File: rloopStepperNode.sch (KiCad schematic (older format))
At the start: 0 parts

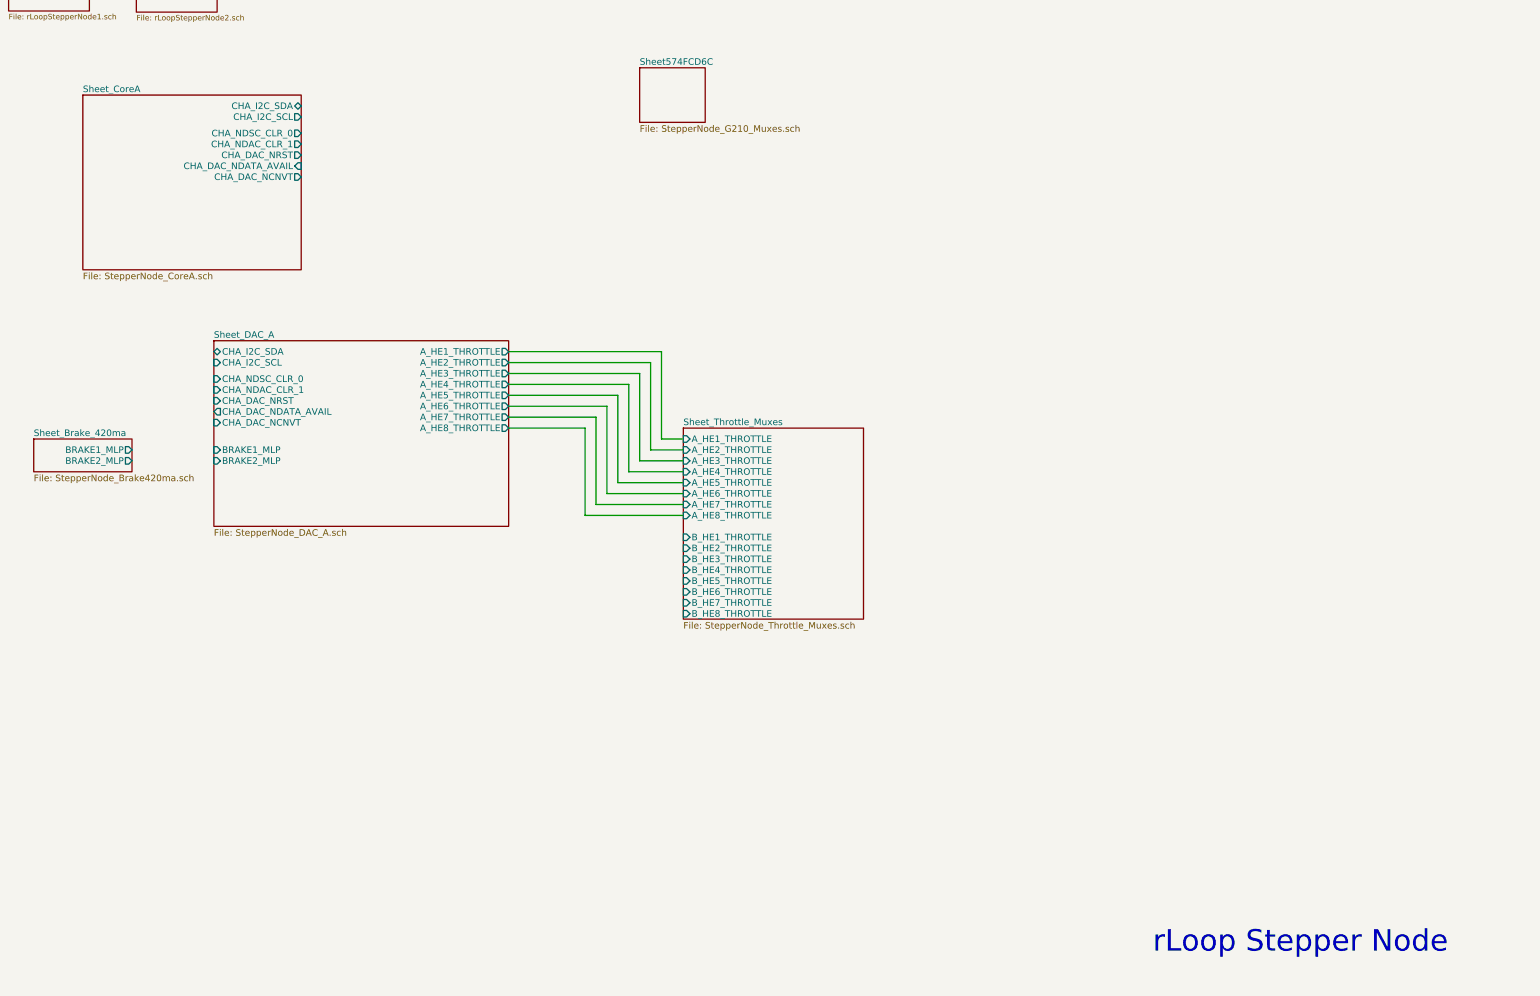
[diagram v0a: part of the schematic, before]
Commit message: Setup DAC channel B
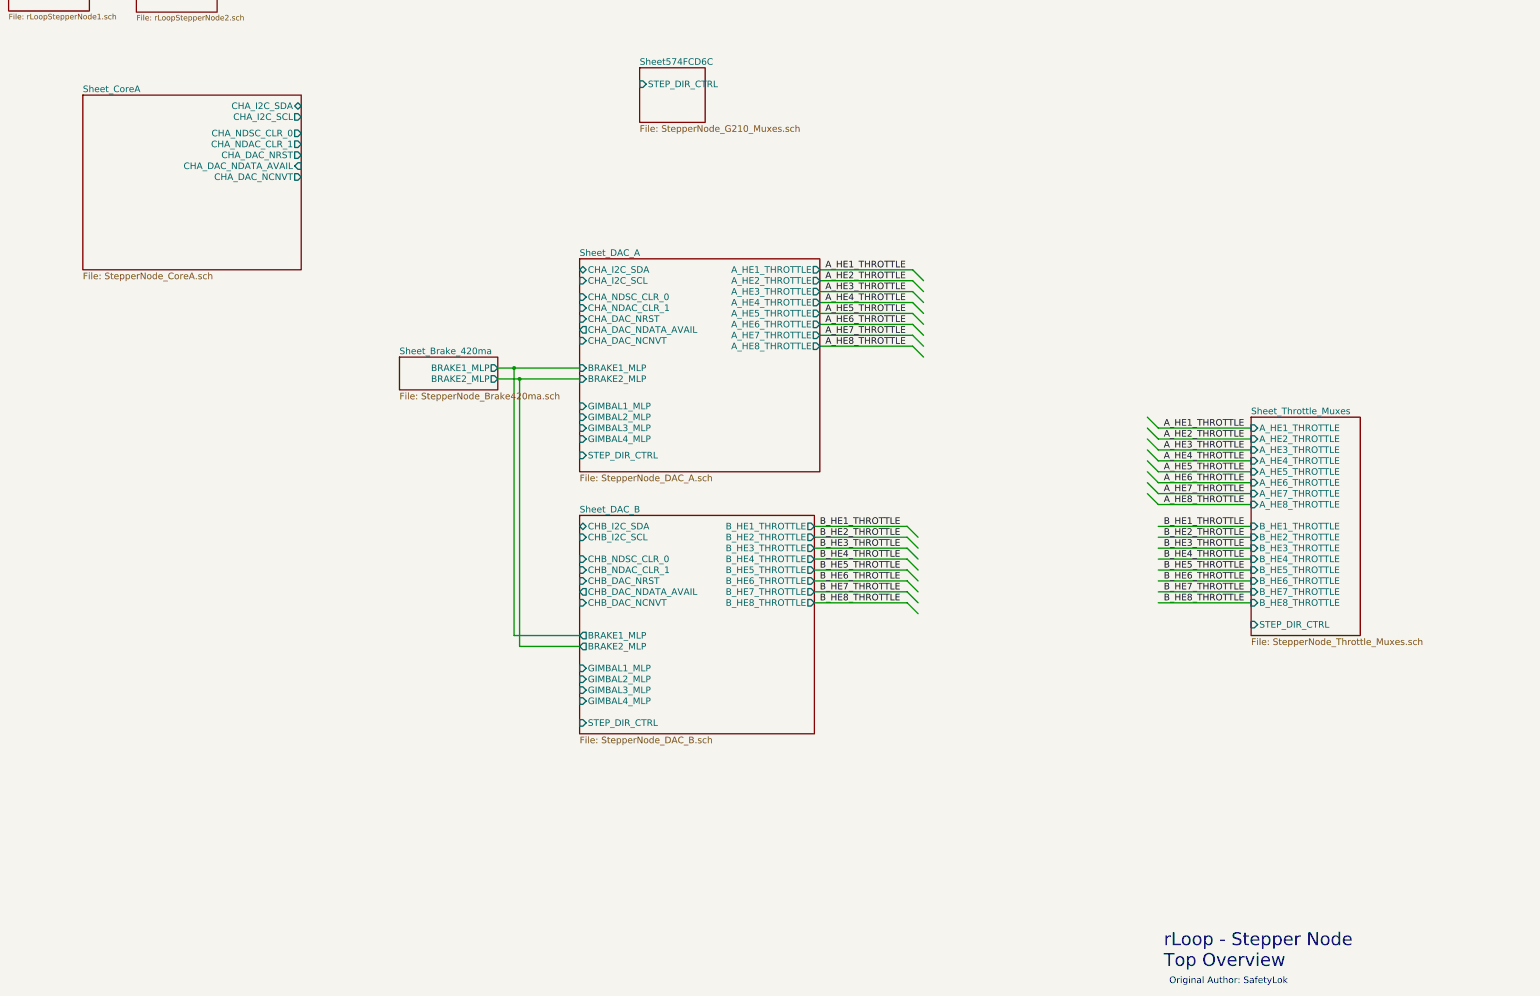
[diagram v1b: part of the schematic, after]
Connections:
- net labels added: A_HE1_THROTTLE, A_HE2_THROTTLE, A_HE3_THROTTLE, A_HE4_THROTTLE, A_HE5_THROTTLE, A_HE6_THROTTLE, A_HE7_THROTTLE, A_HE8_THROTTLE, B_HE1_THROTTLE, B_HE2_THROTTLE, B_HE3_THROTTLE, B_HE4_THROTTLE, B_HE5_THROTTLE, B_HE6_THROTTLE, B_HE7_THROTTLE, B_HE8_THROTTLE
- wire segments 24 -> 38
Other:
- note added: "Original Author: SafetyLok"
- note added: "rLoop - Stepper Node\nTop Overview\n"
- note removed: "rLoop Stepper Node\n"

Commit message: Setup Node Core Channel B
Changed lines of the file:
@@
 $Descr A3 16535 11693
 encoding utf-8
-Sheet 1 9
+Sheet 1 11
 Title "Top Level"
 Date ""
@@
 $EndDescr
 $Sheet
-S 1320 1150 740  430
-U 570CA0E2
-F0 "Sheet1" 50
-F1 "rLoopStepperNode1.sch" 50
-$EndSheet
-$Sheet
-S 2490 1150 740  440
-U 570DA2A0
-F0 "Sheet2" 50
-F1 "rLoopStepperNode2.sch" 50
-$EndSheet
-$Sheet
-S 7100 2100 600  500
+S 12700 3450 950  600
 U 574FCD6D
-F0 "Sheet574FCD6C" 60
+F0 "Sheet_G210_Muxes" 60
 F1 "StepperNode_G210_Muxes.sch" 60
-F2 "STEP_DIR_CTRL" I L 7100 2250 60
-$EndSheet
-$Sheet
-S 2000 2350 2000 1600
-U 57538643
-F0 "Sheet_CoreA" 60
-F1 "StepperNode_CoreA.sch" 60
-F2 "CHA_I2C_SDA" B R 4000 2450 60
-F3 "CHA_I2C_SCL" O R 4000 2550 60
-F4 "CHA_NDSC_CLR_0" O R 4000 2700 60
-F5 "CHA_NDAC_CLR_1" O R 4000 2800 60
-F6 "CHA_DAC_NRST" O R 4000 2900 60
-F7 "CHA_DAC_NDATA_AVAIL" I R 4000 3000 60
-F8 "CHA_DAC_NCNVT" O R 4000 3100 60
+F2 "STEP_DIR_CTRL" I L 12700 3600 60
 $EndSheet
 $Sheet
@@
 Text Notes 11950 10500 0    60   ~ 0
 Original Author: SafetyLok
+$Sheet
+S 12700 1800 900  1150
+U 5754F8C0
+F0 "Sheet_Gimbal_Sw" 60
+F1 "StepperNode_Gimbal_Switches.sch" 60
+$EndSheet
+$Sheet
+S 2000 5850 1250 2200
+U 57556833
+F0 "Sheet_CoreB" 60
+F1 "StepperNode_CoreB.sch" 60
+F2 "CHB_I2C_SDA" B R 3250 5950 60
+F3 "CHB_I2C_SCL" O R 3250 6050 60
+F4 "CHB_NDSC_CLR_0" O R 3250 6200 60
+F5 "CHB_NDAC_CLR_1" O R 3250 6300 60
+F6 "CHB_DAC_NRST" O R 3250 6400 60
+F7 "CHB_DAC_NDATA_AVAIL" I R 3250 6500 60
+F8 "CHB_DAC_NCNVT" O R 3250 6600 60
+F9 "CHB_STEP1_DIR" O R 3250 6800 60
+F10 "CHB_STEP1_STEP" O R 3250 6900 60
+F11 "CHB_STEP2_DIR" O R 3250 7000 60
+F12 "CHB_STEP2_STEP" O R 3250 7100 60
+F13 "CHB_STEP3_DIR" O R 3250 7200 60
+F14 "CHB_STEP3_STEP" O R 3250 7300 60
+F15 "CHB_STEP4_DIR" O R 3250 7400 60
+F16 "CHB_STEP4_STEP" O R 3250 7500 60
+F17 "CHB_STEP5_DIR" O R 3250 7600 60
+F18 "CHB_STEP5_STEP" O R 3250 7700 60
+F19 "CHB_STEP6_DIR" O R 3250 7800 60
+F20 "CHB_STEP6_STEP" O R 3250 7900 60
+$EndSheet
+$Sheet
+S 2000 2350 1250 2450
+U 57538643
+F0 "Sheet_CoreA" 60
+F1 "StepperNode_CoreA.sch" 60
+F2 "CHA_I2C_SDA" B R 3250 2450 60
+F3 "CHA_I2C_SCL" O R 3250 2550 60
+F4 "CHA_NDSC_CLR_0" O R 3250 2700 60
+F5 "CHA_NDAC_CLR_1" O R 3250 2800 60
+F6 "CHA_DAC_NRST" O R 3250 2900 60
+F7 "CHA_DAC_NDATA_AVAIL" I R 3250 3000 60
+F8 "CHA_DAC_NCNVT" O R 3250 3100 60
+F9 "CHA_STEP1_DIR" O R 3250 3350 60
+F10 "CHA_STEP1_STEP" O R 3250 3450 60
+F11 "CHA_STEP2_DIR" O R 3250 3550 60
+F12 "CHA_STEP2_STEP" O R 3250 3650 60
+F13 "CHA_STEP3_DIR" O R 3250 3750 60
+F14 "CHA_STEP3_STEP" O R 3250 3850 60
+F15 "CHA_STEP4_DIR" O R 3250 3950 60
+F16 "CHA_STEP4_STEP" O R 3250 4050 60
+F17 "CHA_STEP5_DIR" O R 3250 4150 60
+F18 "CHA_STEP5_STEP" O R 3250 4250 60
+F19 "CHA_STEP6_DIR" O R 3250 4350 60
+F20 "CHA_STEP6_STEP" O R 3250 4450 60
+$EndSheet
 $EndSCHEMATC

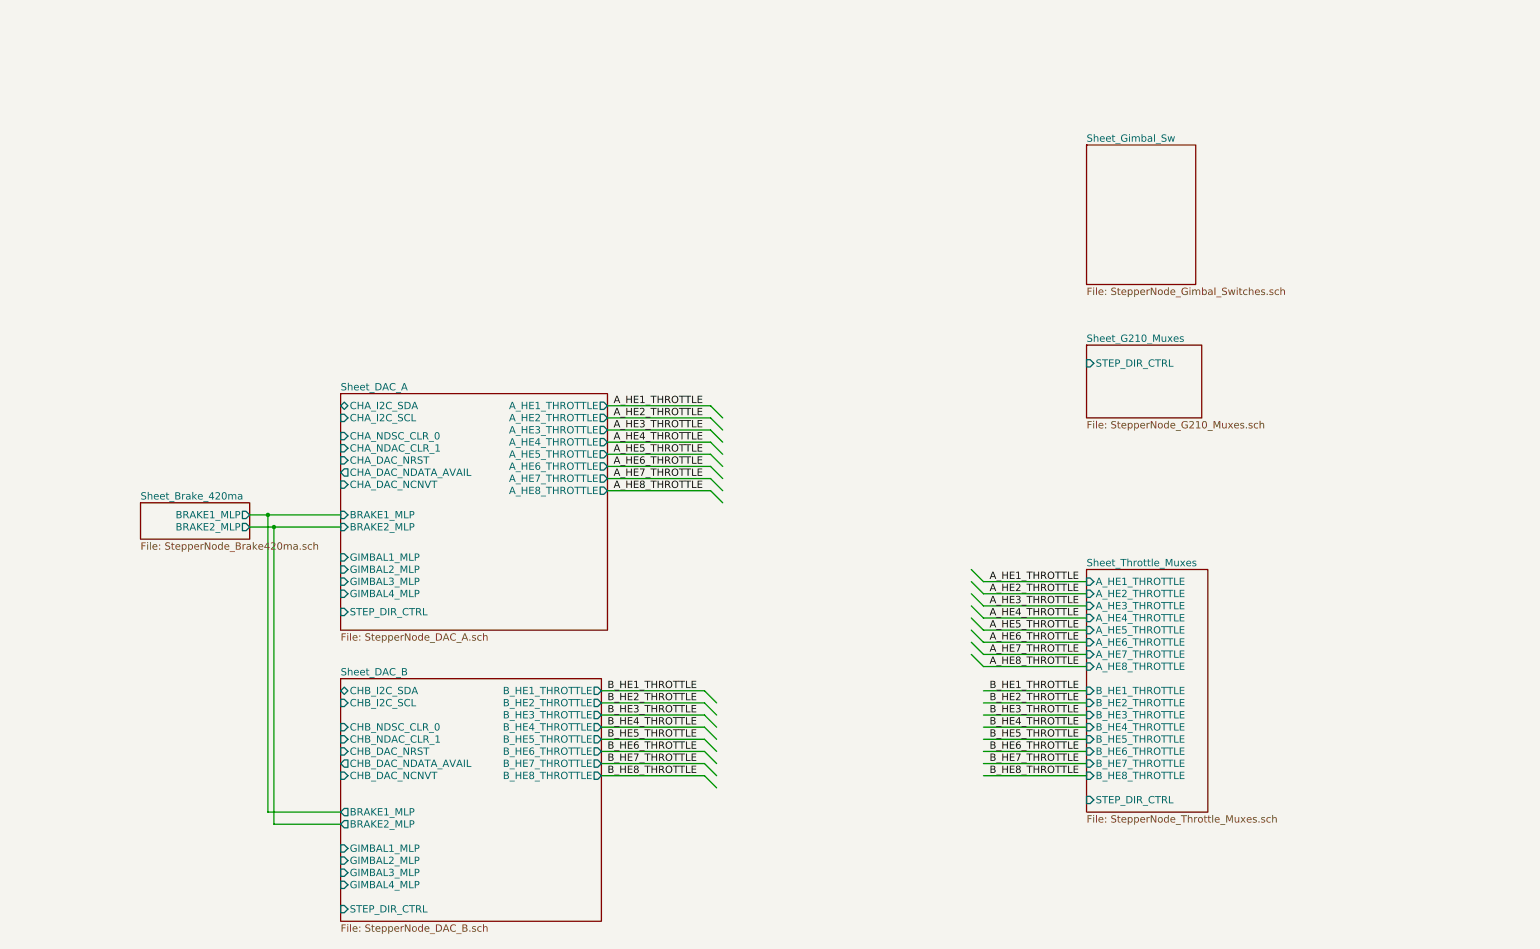
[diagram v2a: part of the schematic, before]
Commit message: Added Sheets for Gimbal, Pusher Interlock and Accels
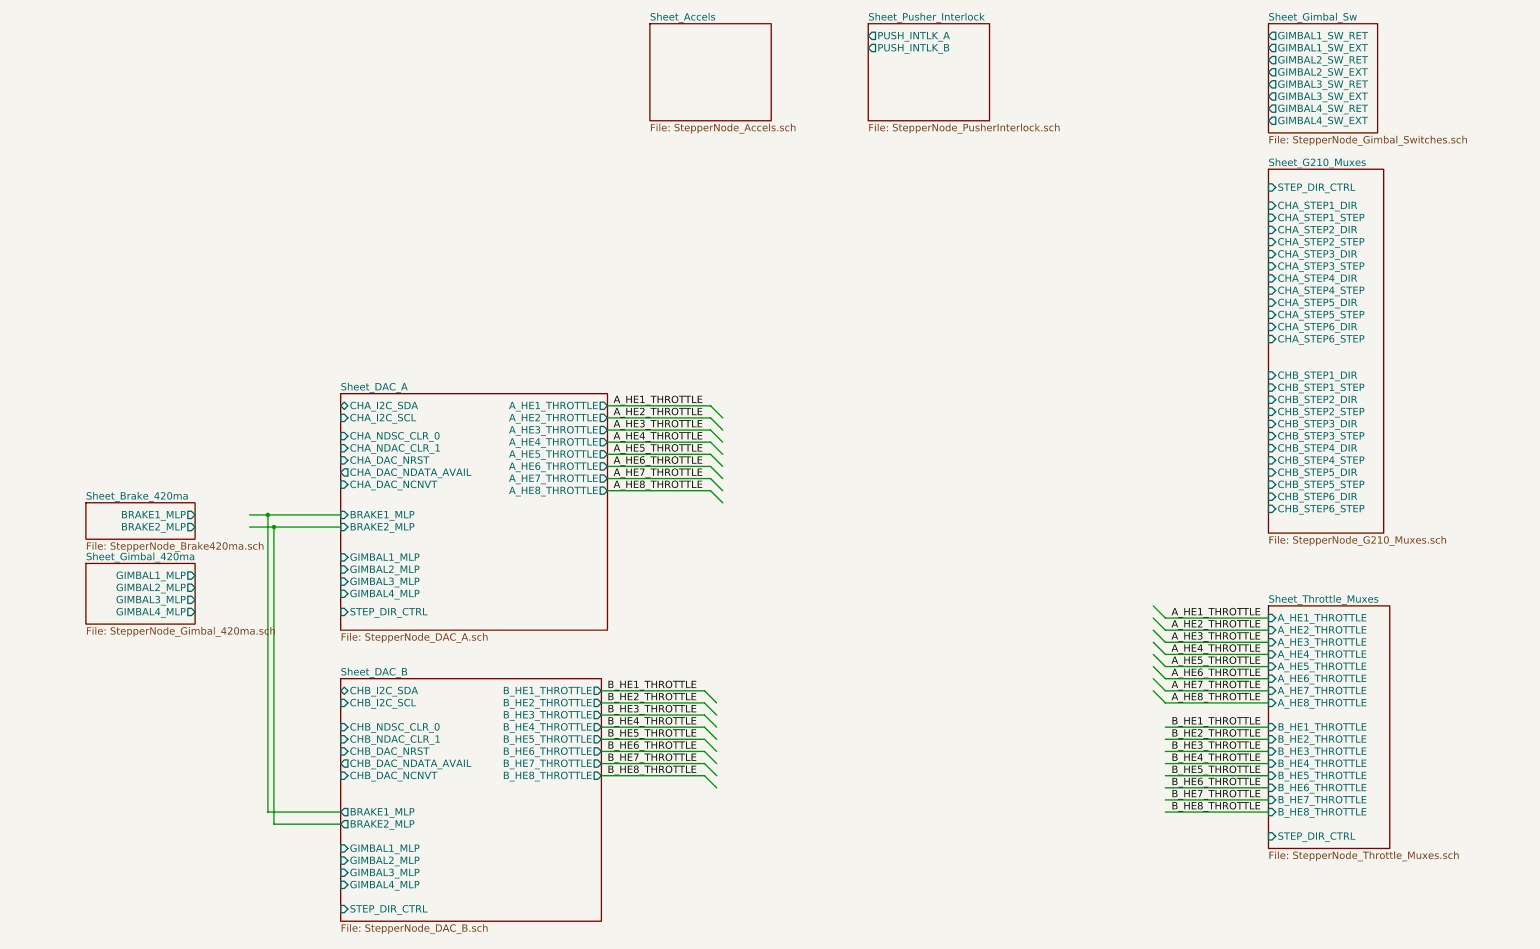
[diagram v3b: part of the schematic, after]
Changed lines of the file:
@@
 $Descr A3 16535 11693
 encoding utf-8
-Sheet 1 11
+Sheet 1 12
 Title "Top Level"
 Date ""
@@
 $EndDescr
 $Sheet
-S 12700 3450 950  600
+S 14200 2000 950  3000
 U 574FCD6D
 F0 "Sheet_G210_Muxes" 60
 F1 "StepperNode_G210_Muxes.sch" 60
-F2 "STEP_DIR_CTRL" I L 12700 3600 60
+F2 "STEP_DIR_CTRL" I L 14200 2150 60
+F3 "CHA_STEP1_DIR" I L 14200 2300 60
+F4 "CHA_STEP1_STEP" I L 14200 2400 60
+F5 "CHB_STEP2_DIR" I L 14200 3900 60
+F6 "CHA_STEP2_STEP" I L 14200 2600 60
+F7 "CHB_STEP1_DIR" I L 14200 3700 60
+F8 "CHB_STEP1_STEP" I L 14200 3800 60
+F9 "CHA_STEP2_DIR" I L 14200 2500 60
+F10 "CHB_STEP2_STEP" I L 14200 4000 60
+F11 "CHA_STEP3_DIR" I L 14200 2700 60
+F12 "CHA_STEP3_STEP" I L 14200 2800 60
+F13 "CHB_STEP3_DIR" I L 14200 4100 60
+F14 "CHB_STEP3_STEP" I L 14200 4200 60
+F15 "CHB_STEP4_DIR" I L 14200 4300 60
+F16 "CHA_STEP4_STEP" I L 14200 3000 60
+F17 "CHA_STEP4_DIR" I L 14200 2900 60
+F18 "CHB_STEP4_STEP" I L 14200 4400 60
+F19 "CHA_STEP5_DIR" I L 14200 3100 60
+F20 "CHA_STEP5_STEP" I L 14200 3200 60
+F21 "CHB_STEP5_DIR" I L 14200 4500 60
+F22 "CHB_STEP5_STEP" I L 14200 4600 60
+F23 "CHB_STEP6_DIR" I L 14200 4700 60
+F24 "CHA_STEP6_STEP" I L 14200 3400 60
+F25 "CHA_STEP6_DIR" I L 14200 3300 60
+F26 "CHB_STEP6_STEP" I L 14200 4800 60
 $EndSheet
 $Sheet
@@
 $EndSheet
 $Sheet
-S 4900 4750 900  300
+S 4450 4750 900  300
 U 57538173
 F0 "Sheet_Brake_420ma" 60
 F1 "StepperNode_Brake420ma.sch" 60
-F2 "BRAKE1_MLP" O R 5800 4850 60
-F3 "BRAKE2_MLP" O R 5800 4950 60
-$EndSheet
-$Sheet
-S 12700 5300 1000 2000
+F2 "BRAKE1_MLP" O R 5350 4850 60
+F3 "BRAKE2_MLP" O R 5350 4950 60
+$EndSheet
+$Sheet
+S 14200 5600 1000 2000
 U 5753BE5C
 F0 "Sheet_Throttle_Muxes" 60
 F1 "StepperNode_Throttle_Muxes.sch" 60
-F2 "A_HE1_THROTTLE" I L 12700 5400 60
-F3 "B_HE1_THROTTLE" I L 12700 6300 60
-F4 "A_HE2_THROTTLE" I L 12700 5500 60
-F5 "B_HE2_THROTTLE" I L 12700 6400 60
-F6 "A_HE3_THROTTLE" I L 12700 5600 60
-F7 "B_HE3_THROTTLE" I L 12700 6500 60
-F8 "A_HE4_THROTTLE" I L 12700 5700 60
-F9 "B_HE4_THROTTLE" I L 12700 6600 60
-F10 "A_HE5_THROTTLE" I L 12700 5800 60
-F11 "B_HE5_THROTTLE" I L 12700 6700 60
-F12 "A_HE6_THROTTLE" I L 12700 5900 60
-F13 "B_HE6_THROTTLE" I L 12700 6800 60
-F14 "A_HE7_THROTTLE" I L 12700 6000 60
-F15 "B_HE7_THROTTLE" I L 12700 6900 60
-F16 "A_HE8_THROTTLE" I L 12700 6100 60
-F17 "B_HE8_THROTTLE" I L 12700 7000 60
-F18 "STEP_DIR_CTRL" I L 12700 7200 60
-$EndSheet
-Wire Wire Line
-	11850 5400 12700 5400
-Text Label 11900 5400 0    60   ~ 0
+F2 "A_HE1_THROTTLE" I L 14200 5700 60
+F3 "B_HE1_THROTTLE" I L 14200 6600 60
+F4 "A_HE2_THROTTLE" I L 14200 5800 60
+F5 "B_HE2_THROTTLE" I L 14200 6700 60
+F6 "A_HE3_THROTTLE" I L 14200 5900 60
+F7 "B_HE3_THROTTLE" I L 14200 6800 60
+F8 "A_HE4_THROTTLE" I L 14200 6000 60
+F9 "B_HE4_THROTTLE" I L 14200 6900 60
+F10 "A_HE5_THROTTLE" I L 14200 6100 60
+F11 "B_HE5_THROTTLE" I L 14200 7000 60
+F12 "A_HE6_THROTTLE" I L 14200 6200 60
+F13 "B_HE6_THROTTLE" I L 14200 7100 60
+F14 "A_HE7_THROTTLE" I L 14200 6300 60
+F15 "B_HE7_THROTTLE" I L 14200 7200 60
+F16 "A_HE8_THROTTLE" I L 14200 6400 60
+F17 "B_HE8_THROTTLE" I L 14200 7300 60
+F18 "STEP_DIR_CTRL" I L 14200 7500 60
+$EndSheet
+Wire Wire Line
+	13350 5700 14200 5700
+Text Label 13400 5700 0    60   ~ 0
 A_HE1_THROTTLE
 Wire Wire Line
-	11850 5500 12700 5500
-Text Label 11900 5500 0    60   ~ 0
+	13350 5800 14200 5800
+Text Label 13400 5800 0    60   ~ 0
 A_HE2_THROTTLE
 Wire Wire Line
-	11850 5600 12700 5600
-Text Label 11900 5600 0    60   ~ 0
+	13350 5900 14200 5900
+Text Label 13400 5900 0    60   ~ 0
 A_HE3_THROTTLE
 Wire Wire Line
-	11850 5700 12700 5700
-Text Label 11900 5700 0    60   ~ 0
+	13350 6000 14200 6000
+Text Label 13400 6000 0    60   ~ 0
 A_HE4_THROTTLE
 Wire Wire Line
-	11850 5800 12700 5800
-Text Label 11900 5800 0    60   ~ 0
+	13350 6100 14200 6100
+Text Label 13400 6100 0    60   ~ 0
 A_HE5_THROTTLE
 Wire Wire Line
-	11850 5900 12700 5900
-Text Label 11900 5900 0    60   ~ 0
+	13350 6200 14200 6200
+Text Label 13400 6200 0    60   ~ 0
 A_HE6_THROTTLE
 Wire Wire Line
-	11850 6000 12700 6000
-Text Label 11900 6000 0    60   ~ 0
+	13350 6300 14200 6300
+Text Label 13400 6300 0    60   ~ 0
 A_HE7_THROTTLE
 Wire Wire Line
-	11850 6100 12700 6100
-Text Label 11900 6100 0    60   ~ 0
+	13350 6400 14200 6400
+Text Label 13400 6400 0    60   ~ 0
 A_HE8_THROTTLE
 Entry Wire Line
@@
 	9600 4650 9700 4750
 Entry Wire Line
-	11750 5300 11850 5400
-Entry Wire Line
-	11750 5400 11850 5500
-Entry Wire Line
-	11750 5500 11850 5600
-Entry Wire Line
-	11750 5600 11850 5700
-Entry Wire Line
-	11750 5700 11850 5800
-Entry Wire Line
-	11750 5800 11850 5900
-Entry Wire Line
-	11750 5900 11850 6000
-Entry Wire Line
-	11750 6000 11850 6100
-Wire Wire Line
-	11850 6300 12700 6300
-Text Label 11900 6300 0    60   ~ 0
+	13250 5600 13350 5700
+Entry Wire Line
+	13250 5700 13350 5800
+Entry Wire Line
+	13250 5800 13350 5900
+Entry Wire Line
+	13250 5900 13350 6000
+Entry Wire Line
+	13250 6000 13350 6100
+Entry Wire Line
+	13250 6100 13350 6200
+Entry Wire Line
+	13250 6200 13350 6300
+Entry Wire Line
+	13250 6300 13350 6400
+Wire Wire Line
+	13350 6600 14200 6600
+Text Label 13400 6600 0    60   ~ 0
 B_HE1_THROTTLE
 Wire Wire Line
-	11850 6400 12700 6400
-Text Label 11900 6400 0    60   ~ 0
+	13350 6700 14200 6700
+Text Label 13400 6700 0    60   ~ 0
 B_HE2_THROTTLE
 Wire Wire Line
-	11850 6500 12700 6500
-Text Label 11900 6500 0    60   ~ 0
+	13350 6800 14200 6800
+Text Label 13400 6800 0    60   ~ 0
 B_HE3_THROTTLE
 Wire Wire Line
-	11850 6600 12700 6600
-Text Label 11900 6600 0    60   ~ 0
+	13350 6900 14200 6900
+Text Label 13400 6900 0    60   ~ 0
 B_HE4_THROTTLE
 Wire Wire Line
-	11850 6700 12700 6700
-Text Label 11900 6700 0    60   ~ 0
+	13350 7000 14200 7000
+Text Label 13400 7000 0    60   ~ 0
 B_HE5_THROTTLE
 Wire Wire Line
-	11850 6800 12700 6800
-Text Label 11900 6800 0    60   ~ 0
+	13350 7100 14200 7100
+Text Label 13400 7100 0    60   ~ 0
 B_HE6_THROTTLE
 Wire Wire Line
-	11850 6900 12700 6900
-Text Label 11900 6900 0    60   ~ 0
+	13350 7200 14200 7200
+Text Label 13400 7200 0    60   ~ 0
 B_HE7_THROTTLE
 Wire Wire Line
-	11850 7000 12700 7000
-Text Label 11900 7000 0    60   ~ 0
+	13350 7300 14200 7300
+Text Label 13400 7300 0    60   ~ 0
 B_HE8_THROTTLE
 Wire Wire Line
@@
 Original Author: SafetyLok
 $Sheet
-S 12700 1800 900  1150
+S 14200 800  900  900
 U 5754F8C0
 F0 "Sheet_Gimbal_Sw" 60
 F1 "StepperNode_Gimbal_Switches.sch" 60
+F2 "GIMBAL1_SW_RET" O L 14200 900 60
+F3 "GIMBAL1_SW_EXT" O L 14200 1000 60
+F4 "GIMBAL2_SW_RET" O L 14200 1100 60
+F5 "GIMBAL2_SW_EXT" O L 14200 1200 60
+F6 "GIMBAL3_SW_RET" O L 14200 1300 60
+F7 "GIMBAL3_SW_EXT" O L 14200 1400 60
+F8 "GIMBAL4_SW_RET" O L 14200 1500 60
+F9 "GIMBAL4_SW_EXT" O L 14200 1600 60
 $EndSheet
 $Sheet
@@
 F20 "CHA_STEP6_STEP" O R 3250 4450 60
 $EndSheet
+$Sheet
+S 4450 5250 900  500
+U 5758E2DB
+F0 "Sheet_Gimbal_420ma" 60
+F1 "StepperNode_Gimbal_420ma.sch" 60
+F2 "GIMBAL1_MLP" O R 5350 5350 60
+F3 "GIMBAL2_MLP" O R 5350 5450 60
+F4 "GIMBAL3_MLP" O R 5350 5550 60
+F5 "GIMBAL4_MLP" O R 5350 5650 60
+$EndSheet
+$Sheet
+S 10900 800  1000 800
+U 575CD1E2
+F0 "Sheet_Pusher_Interlock" 60
+F1 "StepperNode_PusherInterlock.sch" 60
+F2 "PUSH_INTLK_A" O L 10900 900 60
+F3 "PUSH_INTLK_B" O L 10900 1000 60
+$EndSheet
+$Sheet
+S 9100 800  1000 800
+U 575DC8CA
+F0 "Sheet_Accels" 60
+F1 "StepperNode_Accels.sch" 60
+$EndSheet
 $EndSCHEMATC
